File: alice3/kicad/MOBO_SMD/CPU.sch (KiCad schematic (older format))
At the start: 8 parts, among them U6 Z80CPU, U7 71V424S15PHGI8

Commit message: Replace Z80 D40 with SMD.
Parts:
- removed U6: Z80CPU, Housings_QFP:LQFP-44_10x10mm_Pitch0.8mm, symbol Z80CPU
- added U?: Z80CPU-SMD, symbol Z80CPU-SMD
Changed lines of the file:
@@
 LIBS:mini_din
 LIBS:24lc256
+LIBS:z80cpu-smd
 LIBS:MOBO_SMD-cache
 EELAYER 25 0
@@
 L GND #PWR47
 U 1 1 568DE0B3
-P 4100 4600
-F 0 "#PWR47" H 4100 4350 50  0001 C CNN
-F 1 "GND" H 4100 4450 50  0000 C CNN
-F 2 "" H 4100 4600 50  0000 C CNN
-F 3 "" H 4100 4600 50  0000 C CNN
-	1    4100 4600
-	1    0    0    -1
-$EndComp
-Wire Wire Line
-	4100 4600 4100 4500
+P 3950 4600
+F 0 "#PWR47" H 3950 4350 50  0001 C CNN
+F 1 "GND" H 3950 4450 50  0000 C CNN
+F 2 "" H 3950 4600 50  0000 C CNN
+F 3 "" H 3950 4600 50  0000 C CNN
+	1    3950 4600
+	1    0    0    -1
+$EndComp
 Wire Wire Line
 	4100 1500 4100 800
@@
 	2200 2050 2200 1800
 Connection ~ 2200 1800
-$Comp
-L Z80CPU U6
-U 1 1 568DDED4
-P 4100 3000
-F 0 "U6" H 3550 4400 50  0000 L CNN
-F 1 "Z80CPU" H 4350 4400 50  0000 L CNN
-F 2 "Housings_QFP:LQFP-44_10x10mm_Pitch0.8mm" H 4100 3400 50  0001 C CNN
-F 3 "" H 4100 3400 50  0000 C CNN
-	1    4100 3000
-	1    0    0    -1
-$EndComp
 Wire Wire Line
 	3150 2100 3400 2100
@@
 	7050 3575 6400 3575
 Connection ~ 6400 3675
+$Comp
+L Z80CPU-SMD U?
+U 1 1 56D385CE
+P 4100 3000
+F 0 "U?" H 3550 4400 50  0000 L CNN
+F 1 "Z80CPU-SMD" H 4200 4400 50  0000 L CNN
+F 2 "" H 4100 3400 50  0000 C CNN
+F 3 "" H 4100 3400 50  0000 C CNN
+	1    4100 3000
+	1    0    0    -1
+$EndComp
+Wire Wire Line
+	3950 4600 3950 4500
 $EndSCHEMATC

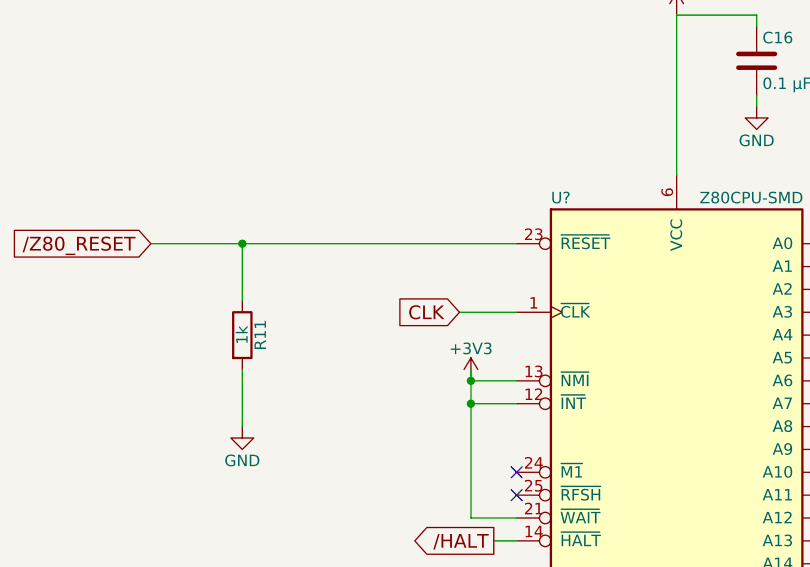
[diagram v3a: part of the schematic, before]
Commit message: Minor fixes to CPU.
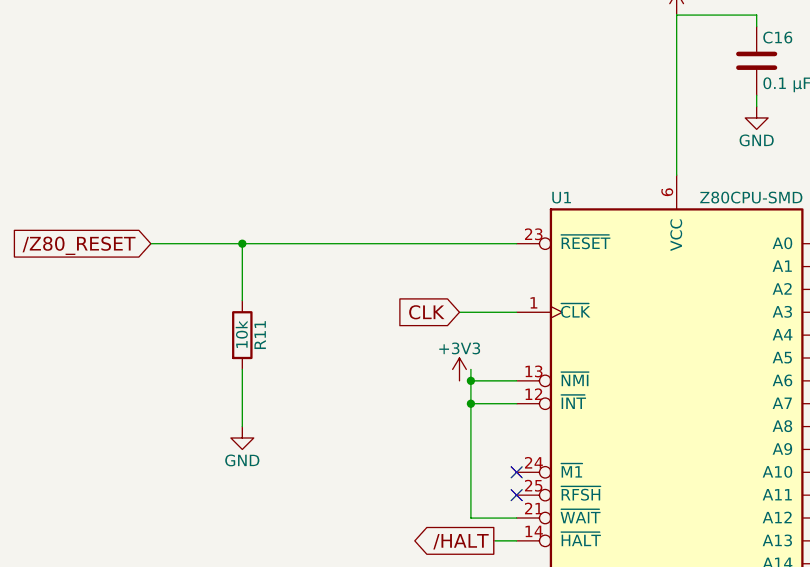
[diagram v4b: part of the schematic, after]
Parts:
- R11: value 1k -> 10k
- gave numbers to parts that had none: 1
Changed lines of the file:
@@
 $EndDescr
 $Comp
-L GND #PWR47
+L GND #PWR46
 U 1 1 568DE0B3
 P 3950 4600
-F 0 "#PWR47" H 3950 4350 50  0001 C CNN
+F 0 "#PWR46" H 3950 4350 50  0001 C CNN
 F 1 "GND" H 3950 4450 50  0000 C CNN
 F 2 "" H 3950 4600 50  0000 C CNN
@@
 P 2200 2200
 F 0 "R11" V 2280 2200 50  0000 C CNN
-F 1 "1k" V 2200 2200 50  0000 C CNN
+F 1 "10k" V 2200 2200 50  0000 C CNN
 F 2 "Resistors_SMD:R_0805" V 2130 2200 50  0001 C CNN
 F 3 "" H 2200 2200 50  0000 C CNN
@@
 	9550 3250 9550 3400
 $Comp
-L +3V3 #PWR46
+L +3V3 #PWR47
 U 1 1 56A5493F
 P 4100 800
-F 0 "#PWR46" H 4100 650 50  0001 C CNN
+F 0 "#PWR47" H 4100 650 50  0001 C CNN
 F 1 "+3V3" H 4100 940 50  0000 C CNN
 F 2 "" H 4100 800 60  0000 C CNN
@@
 L +3V3 #PWR45
 U 1 1 56A55184
-P 3200 2400
-F 0 "#PWR45" H 3200 2250 50  0001 C CNN
-F 1 "+3V3" H 3200 2540 50  0000 C CNN
-F 2 "" H 3200 2400 60  0000 C CNN
-F 3 "" H 3200 2400 60  0000 C CNN
-	1    3200 2400
+P 3150 2400
+F 0 "#PWR45" H 3150 2250 50  0001 C CNN
+F 1 "+3V3" H 3150 2540 50  0000 C CNN
+F 2 "" H 3150 2400 60  0000 C CNN
+F 3 "" H 3150 2400 60  0000 C CNN
+	1    3150 2400
 	1    0    0    -1
 $EndComp
@@
 Connection ~ 6400 3675
 $Comp
-L Z80CPU-SMD U?
+L Z80CPU-SMD U1
 U 1 1 56D385CE
 P 4100 3000
-F 0 "U?" H 3550 4400 50  0000 L CNN
+F 0 "U1" H 3550 4400 50  0000 L CNN
 F 1 "Z80CPU-SMD" H 4200 4400 50  0000 L CNN
 F 2 "" H 4100 3400 50  0000 C CNN

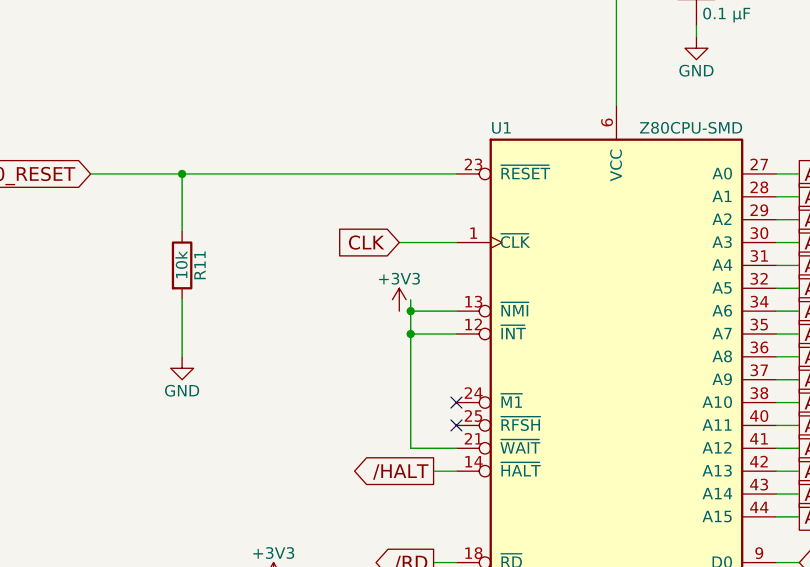
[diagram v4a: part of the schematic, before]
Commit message: Replace Propeller with Q44 version. Remove Prop debug LED.
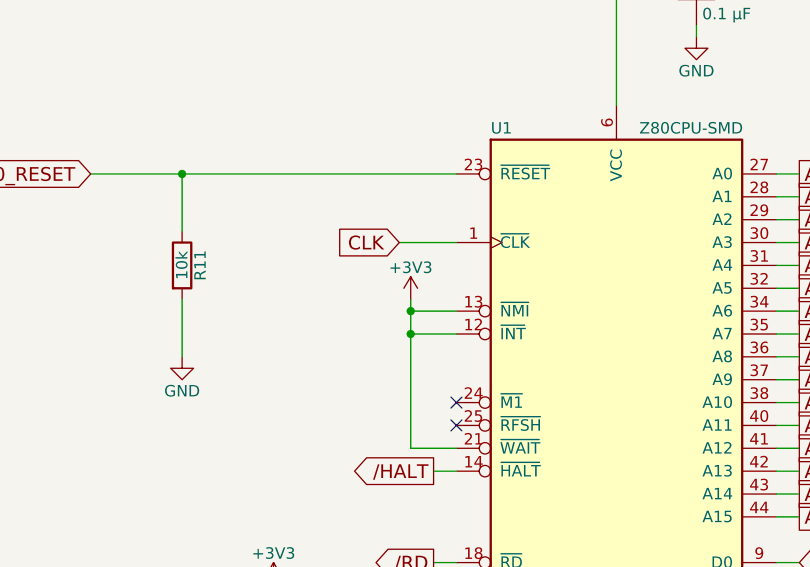
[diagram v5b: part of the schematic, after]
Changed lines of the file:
@@
 LIBS:24lc256
 LIBS:z80cpu-smd
+LIBS:propeller_p8x32a-q44
 LIBS:MOBO_SMD-cache
 EELAYER 25 0
@@
 $EndDescr
 $Comp
-L GND #PWR46
+L GND #PWR44
 U 1 1 568DE0B3
 P 3950 4600
-F 0 "#PWR46" H 3950 4350 50  0001 C CNN
+F 0 "#PWR44" H 3950 4350 50  0001 C CNN
 F 1 "GND" H 3950 4450 50  0000 C CNN
 F 2 "" H 3950 4600 50  0000 C CNN
@@
 /Z80_RESET
 $Comp
-L GND #PWR43
+L GND #PWR41
 U 1 1 568DF463
 P 2200 2600
-F 0 "#PWR43" H 2200 2350 50  0001 C CNN
+F 0 "#PWR41" H 2200 2350 50  0001 C CNN
 F 1 "GND" H 2200 2450 50  0000 C CNN
 F 2 "" H 2200 2600 50  0000 C CNN
@@
 $EndComp
 $Comp
-L GND #PWR50
+L GND #PWR48
 U 1 1 56A01480
 P 6400 5050
-F 0 "#PWR50" H 6400 4800 50  0001 C CNN
+F 0 "#PWR48" H 6400 4800 50  0001 C CNN
 F 1 "GND" H 6400 4900 50  0000 C CNN
 F 2 "" H 6400 5050 50  0000 C CNN
@@
 	3300 3100 3400 3100
 $Comp
-L GND #PWR48
+L GND #PWR46
 U 1 1 56A06CAB
 P 4450 1200
-F 0 "#PWR48" H 4450 950 50  0001 C CNN
+F 0 "#PWR46" H 4450 950 50  0001 C CNN
 F 1 "GND" H 4450 1050 50  0000 C CNN
 F 2 "" H 4450 1200 50  0000 C CNN
@@
 $EndComp
 $Comp
-L GND #PWR56
+L GND #PWR54
 U 1 1 56A06F73
 P 9550 3800
-F 0 "#PWR56" H 9550 3550 50  0001 C CNN
+F 0 "#PWR54" H 9550 3550 50  0001 C CNN
 F 1 "GND" H 9550 3650 50  0000 C CNN
 F 2 "" H 9550 3800 50  0000 C CNN
@@
 	9550 3250 9550 3400
 $Comp
-L +3V3 #PWR47
+L +3V3 #PWR45
 U 1 1 56A5493F
 P 4100 800
-F 0 "#PWR47" H 4100 650 50  0001 C CNN
+F 0 "#PWR45" H 4100 650 50  0001 C CNN
 F 1 "+3V3" H 4100 940 50  0000 C CNN
 F 2 "" H 4100 800 60  0000 C CNN
@@
 $EndComp
 $Comp
-L +3V3 #PWR55
+L +3V3 #PWR53
 U 1 1 56A549BD
 P 9550 3250
-F 0 "#PWR55" H 9550 3100 50  0001 C CNN
+F 0 "#PWR53" H 9550 3100 50  0001 C CNN
 F 1 "+3V3" H 9550 3390 50  0000 C CNN
 F 2 "" H 9550 3250 60  0000 C CNN
@@
 $EndComp
 $Comp
-L +3V3 #PWR45
+L +3V3 #PWR43
 U 1 1 56A55184
-P 3150 2400
-F 0 "#PWR45" H 3150 2250 50  0001 C CNN
-F 1 "+3V3" H 3150 2540 50  0000 C CNN
-F 2 "" H 3150 2400 60  0000 C CNN
-F 3 "" H 3150 2400 60  0000 C CNN
-	1    3150 2400
-	1    0    0    -1
-$EndComp
-$Comp
-L +3V3 #PWR44
+P 3200 2350
+F 0 "#PWR43" H 3200 2200 50  0001 C CNN
+F 1 "+3V3" H 3200 2490 50  0000 C CNN
+F 2 "" H 3200 2350 60  0000 C CNN
+F 3 "" H 3200 2350 60  0000 C CNN
+	1    3200 2350
+	1    0    0    -1
+$EndComp
+$Comp
+L +3V3 #PWR42
 U 1 1 56A551C0
 P 2600 3600
-F 0 "#PWR44" H 2600 3450 50  0001 C CNN
+F 0 "#PWR42" H 2600 3450 50  0001 C CNN
 F 1 "+3V3" H 2600 3740 50  0000 C CNN
 F 2 "" H 2600 3600 60  0000 C CNN
@@
 D0
 $Comp
-L GND #PWR54
+L GND #PWR52
 U 1 1 56CACC99
 P 7850 4375
-F 0 "#PWR54" H 7850 4125 50  0001 C CNN
+F 0 "#PWR52" H 7850 4125 50  0001 C CNN
 F 1 "GND" H 7850 4225 50  0000 C CNN
 F 2 "" H 7850 4375 50  0000 C CNN
@@
 $EndComp
 $Comp
-L GND #PWR52
+L GND #PWR50
 U 1 1 56CACCBC
 P 7650 4375
-F 0 "#PWR52" H 7650 4125 50  0001 C CNN
+F 0 "#PWR50" H 7650 4125 50  0001 C CNN
 F 1 "GND" H 7650 4225 50  0000 C CNN
 F 2 "" H 7650 4375 50  0000 C CNN
@@
 $EndComp
 $Comp
-L GND #PWR58
+L GND #PWR56
 U 1 1 56CACD29
 P 9975 3800
-F 0 "#PWR58" H 9975 3550 50  0001 C CNN
+F 0 "#PWR56" H 9975 3550 50  0001 C CNN
 F 1 "GND" H 9975 3650 50  0000 C CNN
 F 2 "" H 9975 3800 50  0000 C CNN
@@
 	9975 3250 9975 3400
 $Comp
-L +3V3 #PWR57
+L +3V3 #PWR55
 U 1 1 56CACD31
 P 9975 3250
-F 0 "#PWR57" H 9975 3100 50  0001 C CNN
+F 0 "#PWR55" H 9975 3100 50  0001 C CNN
 F 1 "+3V3" H 9975 3390 50  0000 C CNN
 F 2 "" H 9975 3250 60  0000 C CNN
@@
 $EndComp
 $Comp
-L +3V3 #PWR51
+L +3V3 #PWR49
 U 1 1 56CACE05
 P 7650 1575
-F 0 "#PWR51" H 7650 1425 50  0001 C CNN
+F 0 "#PWR49" H 7650 1425 50  0001 C CNN
 F 1 "+3V3" H 7650 1715 50  0000 C CNN
 F 2 "" H 7650 1575 60  0000 C CNN
@@
 $EndComp
 $Comp
-L +3V3 #PWR53
+L +3V3 #PWR51
 U 1 1 56CACEC8
 P 7850 1575
-F 0 "#PWR53" H 7850 1425 50  0001 C CNN
+F 0 "#PWR51" H 7850 1425 50  0001 C CNN
 F 1 "+3V3" H 7850 1715 50  0000 C CNN
 F 2 "" H 7850 1575 60  0000 C CNN
@@
 $EndComp
 $Comp
-L GND #PWR49
+L GND #PWR47
 U 1 1 56CACF44
 P 6400 3750
-F 0 "#PWR49" H 6400 3500 50  0001 C CNN
+F 0 "#PWR47" H 6400 3500 50  0001 C CNN
 F 1 "GND" H 6400 3600 50  0000 C CNN
 F 2 "" H 6400 3750 50  0000 C CNN

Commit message: Replace SRAM with 256 KB.
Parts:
- removed U7: 71V424S15PHGI8, TSOP44-II:TSOP44-II, symbol 71V424S15PHGI8
- added U6: AS6C2008_TSOP, symbol AS6C2008_TSOP
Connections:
- net labels added: A17
- wire segments 56 -> 55
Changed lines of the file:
@@
 LIBS:z80cpu-smd
 LIBS:propeller_p8x32a-q44
+LIBS:as6c2008_tsop
 LIBS:MOBO_SMD-cache
 EELAYER 25 0
@@
 $EndDescr
 $Comp
-L GND #PWR44
+L GND #PWR43
 U 1 1 568DE0B3
 P 3950 4600
-F 0 "#PWR44" H 3950 4350 50  0001 C CNN
+F 0 "#PWR43" H 3950 4350 50  0001 C CNN
 F 1 "GND" H 3950 4450 50  0000 C CNN
 F 2 "" H 3950 4600 50  0000 C CNN
@@
 /Z80_RESET
 $Comp
-L GND #PWR41
+L GND #PWR40
 U 1 1 568DF463
 P 2200 2600
-F 0 "#PWR41" H 2200 2350 50  0001 C CNN
+F 0 "#PWR40" H 2200 2350 50  0001 C CNN
 F 1 "GND" H 2200 2450 50  0000 C CNN
 F 2 "" H 2200 2600 50  0000 C CNN
@@
 $EndComp
 $Comp
-L GND #PWR48
+L GND #PWR47
 U 1 1 56A01480
 P 6400 5050
-F 0 "#PWR48" H 6400 4800 50  0001 C CNN
+F 0 "#PWR47" H 6400 4800 50  0001 C CNN
 F 1 "GND" H 6400 4900 50  0000 C CNN
 F 2 "" H 6400 5050 50  0000 C CNN
@@
 	3300 3100 3400 3100
 $Comp
-L GND #PWR46
+L GND #PWR45
 U 1 1 56A06CAB
 P 4450 1200
-F 0 "#PWR46" H 4450 950 50  0001 C CNN
+F 0 "#PWR45" H 4450 950 50  0001 C CNN
 F 1 "GND" H 4450 1050 50  0000 C CNN
 F 2 "" H 4450 1200 50  0000 C CNN
@@
 $EndComp
 $Comp
-L GND #PWR54
+L GND #PWR51
 U 1 1 56A06F73
 P 9550 3800
-F 0 "#PWR54" H 9550 3550 50  0001 C CNN
+F 0 "#PWR51" H 9550 3550 50  0001 C CNN
 F 1 "GND" H 9550 3650 50  0000 C CNN
 F 2 "" H 9550 3800 50  0000 C CNN
@@
 	9550 3250 9550 3400
 $Comp
-L +3V3 #PWR45
+L +3V3 #PWR44
 U 1 1 56A5493F
 P 4100 800
-F 0 "#PWR45" H 4100 650 50  0001 C CNN
+F 0 "#PWR44" H 4100 650 50  0001 C CNN
 F 1 "+3V3" H 4100 940 50  0000 C CNN
 F 2 "" H 4100 800 60  0000 C CNN
@@
 $EndComp
 $Comp
-L +3V3 #PWR53
+L +3V3 #PWR50
 U 1 1 56A549BD
 P 9550 3250
-F 0 "#PWR53" H 9550 3100 50  0001 C CNN
+F 0 "#PWR50" H 9550 3100 50  0001 C CNN
 F 1 "+3V3" H 9550 3390 50  0000 C CNN
 F 2 "" H 9550 3250 60  0000 C CNN
@@
 $EndComp
 $Comp
-L +3V3 #PWR43
+L +3V3 #PWR42
 U 1 1 56A55184
 P 3200 2350
-F 0 "#PWR43" H 3200 2200 50  0001 C CNN
+F 0 "#PWR42" H 3200 2200 50  0001 C CNN
 F 1 "+3V3" H 3200 2490 50  0000 C CNN
 F 2 "" H 3200 2350 60  0000 C CNN
@@
 $EndComp
 $Comp
-L +3V3 #PWR42
+L +3V3 #PWR41
 U 1 1 56A551C0
 P 2600 3600
-F 0 "#PWR42" H 2600 3450 50  0001 C CNN
+F 0 "#PWR41" H 2600 3450 50  0001 C CNN
 F 1 "+3V3" H 2600 3740 50  0000 C CNN
 F 2 "" H 2600 3600 60  0000 C CNN
@@
 Wire Wire Line
 	6400 4825 6400 5050
-$Comp
-L 71V424S15PHGI8 U7
-U 1 1 56CABEB4
-P 7750 2925
-F 0 "U7" H 7750 3875 50  0000 C CNN
-F 1 "71V424S15PHGI8" H 8250 1625 50  0000 C CNN
-F 2 "TSOP44-II:TSOP44-II" H 7750 2925 50  0001 C CNN
-F 3 "" H 7750 2925 50  0000 C CNN
-	1    7750 2925
-	1    0    0    -1
-$EndComp
 Text GLabel 7050 3375 0    60   Input ~ 0
 A15
@@
 D0
 $Comp
-L GND #PWR52
-U 1 1 56CACC99
-P 7850 4375
-F 0 "#PWR52" H 7850 4125 50  0001 C CNN
-F 1 "GND" H 7850 4225 50  0000 C CNN
-F 2 "" H 7850 4375 50  0000 C CNN
-F 3 "" H 7850 4375 50  0000 C CNN
-	1    7850 4375
-	1    0    0    -1
-$EndComp
-$Comp
-L GND #PWR50
+L GND #PWR49
 U 1 1 56CACCBC
 P 7650 4375
-F 0 "#PWR50" H 7650 4125 50  0001 C CNN
+F 0 "#PWR49" H 7650 4125 50  0001 C CNN
 F 1 "GND" H 7650 4225 50  0000 C CNN
 F 2 "" H 7650 4375 50  0000 C CNN
@@
 $EndComp
 $Comp
-L GND #PWR56
+L GND #PWR53
 U 1 1 56CACD29
 P 9975 3800
-F 0 "#PWR56" H 9975 3550 50  0001 C CNN
+F 0 "#PWR53" H 9975 3550 50  0001 C CNN
 F 1 "GND" H 9975 3650 50  0000 C CNN
 F 2 "" H 9975 3800 50  0000 C CNN
@@
 	9975 3250 9975 3400
 $Comp
-L +3V3 #PWR55
+L +3V3 #PWR52
 U 1 1 56CACD31
 P 9975 3250
-F 0 "#PWR55" H 9975 3100 50  0001 C CNN
+F 0 "#PWR52" H 9975 3100 50  0001 C CNN
 F 1 "+3V3" H 9975 3390 50  0000 C CNN
 F 2 "" H 9975 3250 60  0000 C CNN
@@
 $EndComp
 $Comp
-L +3V3 #PWR49
+L +3V3 #PWR48
 U 1 1 56CACE05
 P 7650 1575
-F 0 "#PWR49" H 7650 1425 50  0001 C CNN
+F 0 "#PWR48" H 7650 1425 50  0001 C CNN
 F 1 "+3V3" H 7650 1715 50  0000 C CNN
 F 2 "" H 7650 1575 60  0000 C CNN
@@
 $EndComp
 $Comp
-L +3V3 #PWR51
-U 1 1 56CACEC8
-P 7850 1575
-F 0 "#PWR51" H 7850 1425 50  0001 C CNN
-F 1 "+3V3" H 7850 1715 50  0000 C CNN
-F 2 "" H 7850 1575 60  0000 C CNN
-F 3 "" H 7850 1575 60  0000 C CNN
-	1    7850 1575
-	1    0    0    -1
-$EndComp
-$Comp
-L GND #PWR47
+L GND #PWR46
 U 1 1 56CACF44
-P 6400 3750
-F 0 "#PWR47" H 6400 3500 50  0001 C CNN
-F 1 "GND" H 6400 3600 50  0000 C CNN
-F 2 "" H 6400 3750 50  0000 C CNN
-F 3 "" H 6400 3750 50  0000 C CNN
-	1    6400 3750
-	1    0    0    -1
-$EndComp
-Wire Wire Line
-	7050 3675 6400 3675
-Wire Wire Line
-	6400 3575 6400 3750
-Wire Wire Line
-	7050 3575 6400 3575
-Connection ~ 6400 3675
+P 6400 3875
+F 0 "#PWR46" H 6400 3625 50  0001 C CNN
+F 1 "GND" H 6400 3725 50  0000 C CNN
+F 2 "" H 6400 3875 50  0000 C CNN
+F 3 "" H 6400 3875 50  0000 C CNN
+	1    6400 3875
+	1    0    0    -1
+$EndComp
 $Comp
 L Z80CPU-SMD U1
@@
 Wire Wire Line
 	3950 4600 3950 4500
+$Comp
+L AS6C2008_TSOP U6
+U 1 1 56D3979F
+P 7750 2925
+F 0 "U6" H 7425 4125 50  0000 C CNN
+F 1 "AS6C2008_TSOP" H 8025 1600 50  0000 C CNN
+F 2 "" H 7750 2925 50  0000 C CNN
+F 3 "" H 7750 2925 50  0000 C CNN
+	1    7750 2925
+	1    0    0    -1
+$EndComp
+Wire Wire Line
+	7050 3775 6400 3775
+Wire Wire Line
+	6400 3775 6400 3875
+Text GLabel 7050 3575 0    60   Input ~ 0
+A17
 $EndSCHEMATC
